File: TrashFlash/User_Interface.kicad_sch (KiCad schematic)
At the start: 15 parts, among them IC7 LP5024RSMR

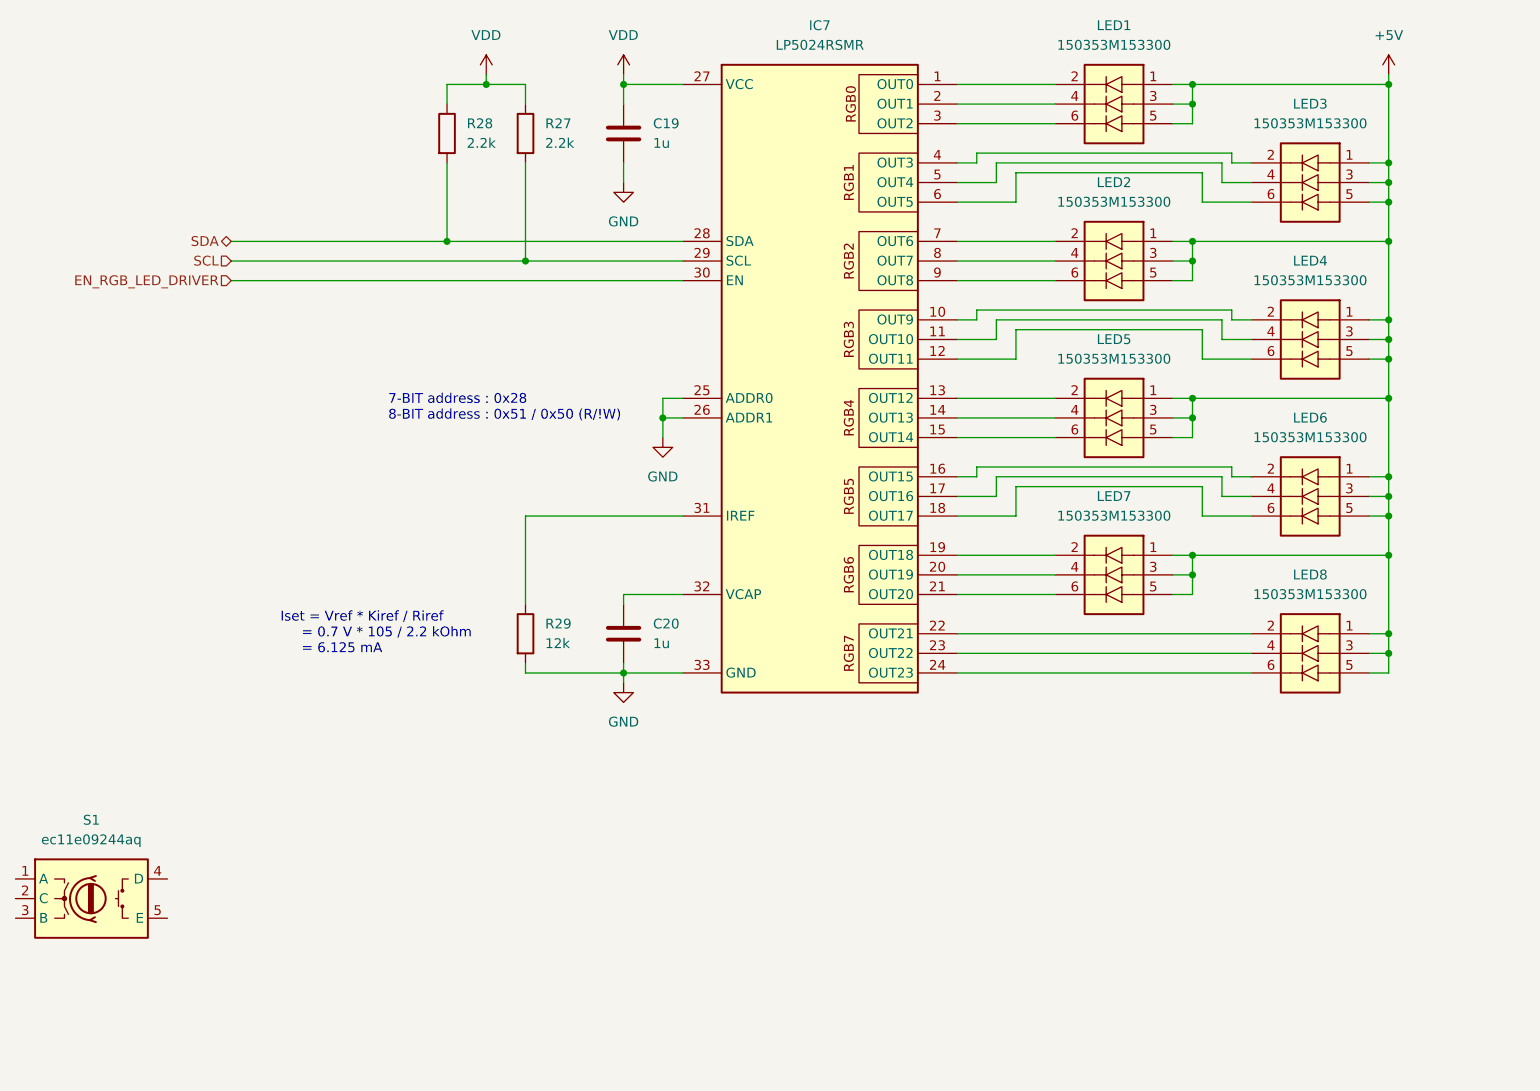
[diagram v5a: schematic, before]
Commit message: Added netlabels / cleaned up schematic
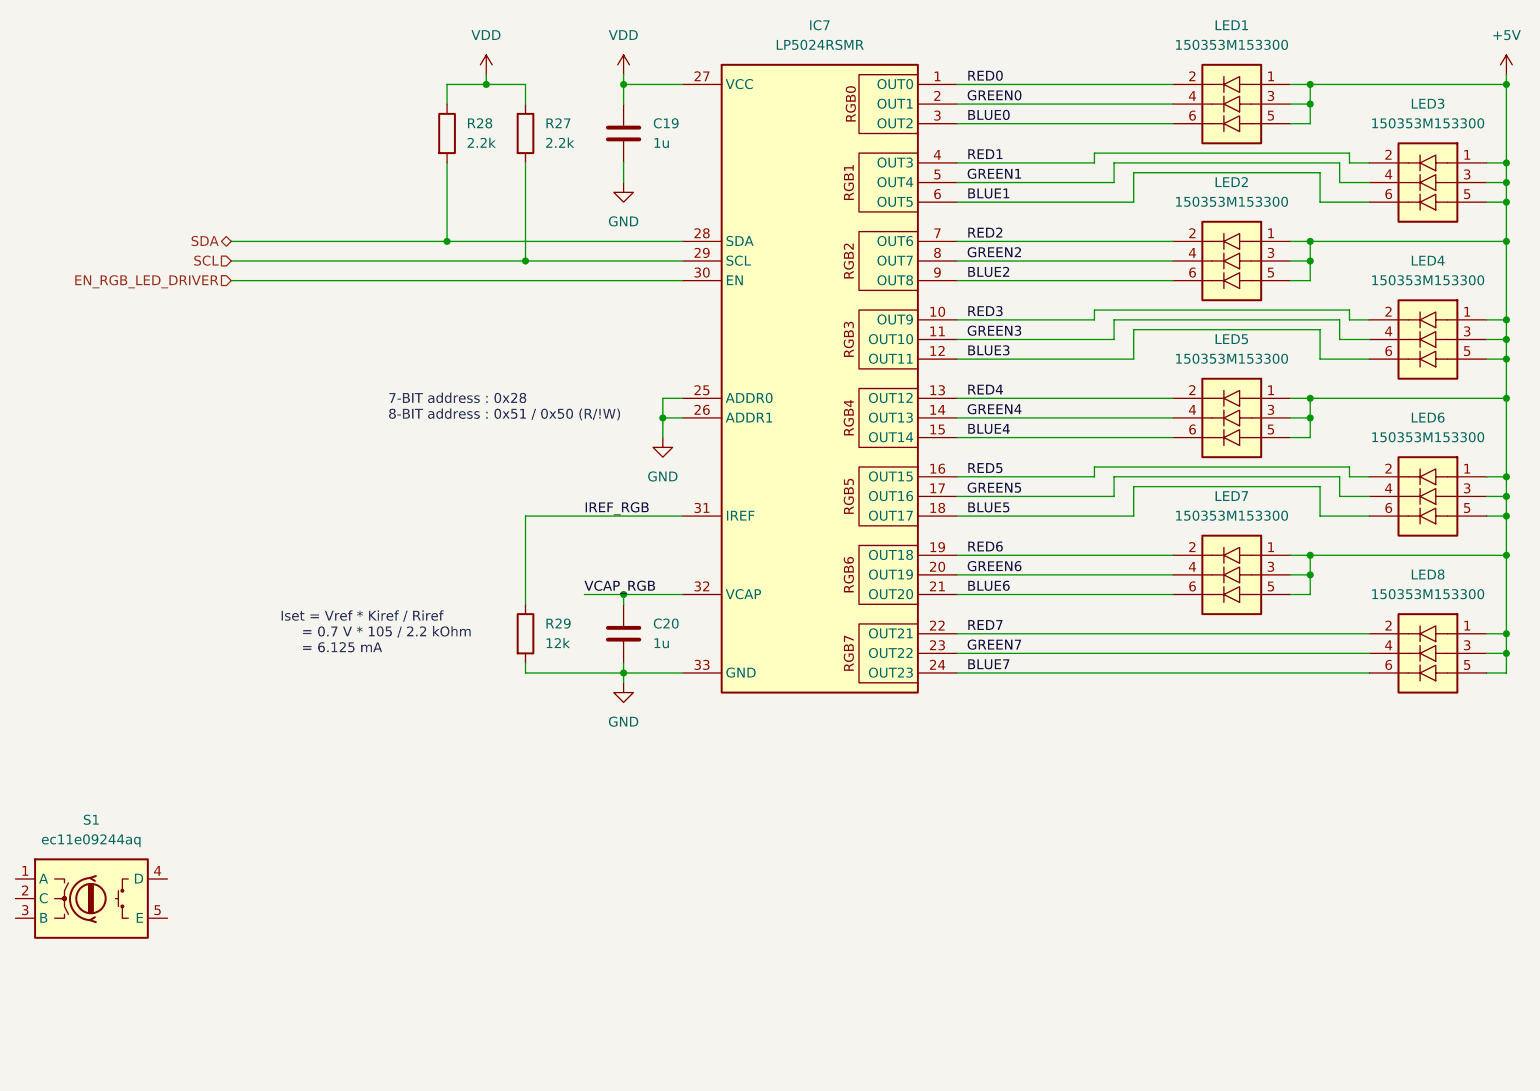
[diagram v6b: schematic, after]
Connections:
- net RED3: now reaches IC7.10 (OUT9), LED4.2 (K_RED)
- net GREEN3: now reaches IC7.11 (OUT10), LED4.4 (K_GREEN)
- net BLUE3: now reaches IC7.12 (OUT11), LED4.6 (K_BLUE)
- net RED2: now reaches IC7.7 (OUT6), LED2.2 (K_RED)
- net GREEN2: now reaches IC7.8 (OUT7), LED2.4 (K_GREEN)
- net BLUE2: now reaches IC7.9 (OUT8), LED2.6 (K_BLUE)
- net RED0: now reaches IC7.1 (OUT0), LED1.2 (K_RED)
- net RED4: now reaches IC7.13 (OUT12), LED5.2 (K_RED)
- net GREEN4: now reaches IC7.14 (OUT13), LED5.4 (K_GREEN)
- net BLUE4: now reaches IC7.15 (OUT14), LED5.6 (K_BLUE)
- net RED5: now reaches IC7.16 (OUT15), LED6.2 (K_RED)
- net GREEN5: now reaches IC7.17 (OUT16), LED6.4 (K_GREEN)
- net BLUE5: now reaches IC7.18 (OUT17), LED6.6 (K_BLUE)
- net RED6: now reaches IC7.19 (OUT18), LED7.2 (K_RED)
- net GREEN0: now reaches IC7.2 (OUT1), LED1.4 (K_GREEN)
- net GREEN6: now reaches IC7.20 (OUT19), LED7.4 (K_GREEN)
- net BLUE6: now reaches IC7.21 (OUT20), LED7.6 (K_BLUE)
- net RED7: now reaches IC7.22 (OUT21), LED8.2 (K_RED)
- net GREEN7: now reaches IC7.23 (OUT22), LED8.4 (K_GREEN)
- net BLUE7: now reaches IC7.24 (OUT23), LED8.6 (K_BLUE)
- net BLUE0: now reaches IC7.3 (OUT2), LED1.6 (K_BLUE)
- net IREF_RGB: now reaches IC7.31 (IREF), R29.1
- net VCAP_RGB: now reaches C20.1, IC7.32 (VCAP)
- net RED1: now reaches IC7.4 (OUT3), LED3.2 (K_RED)
- net GREEN1: now reaches IC7.5 (OUT4), LED3.4 (K_GREEN)
- net BLUE1: now reaches IC7.6 (OUT5), LED3.6 (K_BLUE)
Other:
- moved on the sheet: LED1, LED2, LED3, LED4, LED5, LED6, LED7, LED8

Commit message: Added 3D-models to footprints, PCB outline and component placement
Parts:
- IC7: footprint QFN40P400X400X100-33N-D -> TrashFlash:QFN40P400X400X100-33N-D
- LED1, LED2, LED3, LED4, LED5, LED6, LED7, LED8: footprint 150353M153300 -> TrashFlash:150353M153300
- S1: footprint ec11e09244aq -> TrashFlash:ec11e09244aq
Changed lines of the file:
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@@
 			)
 		)
-		(property "Footprint" "150353M153300"
+		(property "Footprint" "TrashFlash:150353M153300"
 			(at 217.17 166.04 0)
 			(effects
@@
 			)
 		)
-		(property "Footprint" "150353M153300"
+		(property "Footprint" "TrashFlash:150353M153300"
 			(at 191.77 155.88 0)
 			(effects
@@
 			)
 		)
-		(property "Footprint" "ec11e09244aq"
+		(property "Footprint" "TrashFlash:ec11e09244aq"
 			(at 48.26 143.51 0)
 			(effects
@@
 			)
 		)
-		(property "Footprint" "QFN40P400X400X100-33N-D"
+		(property "Footprint" "TrashFlash:QFN40P400X400X100-33N-D"
 			(at 138.43 127 0)
 			(effects
@@
 			)
 		)
-		(property "Footprint" "150353M153300"
+		(property "Footprint" "TrashFlash:150353M153300"
 			(at 217.17 186.36 0)
 			(effects
@@
 			)
 		)
-		(property "Footprint" "150353M153300"
+		(property "Footprint" "TrashFlash:150353M153300"
 			(at 191.77 176.2 0)
 			(effects
@@
 			)
 		)
-		(property "Footprint" "150353M153300"
+		(property "Footprint" "TrashFlash:150353M153300"
 			(at 217.17 145.72 0)
 			(effects
@@
 			)
 		)
-		(property "Footprint" "150353M153300"
+		(property "Footprint" "TrashFlash:150353M153300"
 			(at 217.17 206.68 0)
 			(effects
@@
 			)
 		)
-		(property "Footprint" "150353M153300"
+		(property "Footprint" "TrashFlash:150353M153300"
 			(at 191.77 135.56 0)
 			(effects
@@
 			)
 		)
-		(property "Footprint" "150353M153300"
+		(property "Footprint" "TrashFlash:150353M153300"
 			(at 191.77 196.52 0)
 			(effects

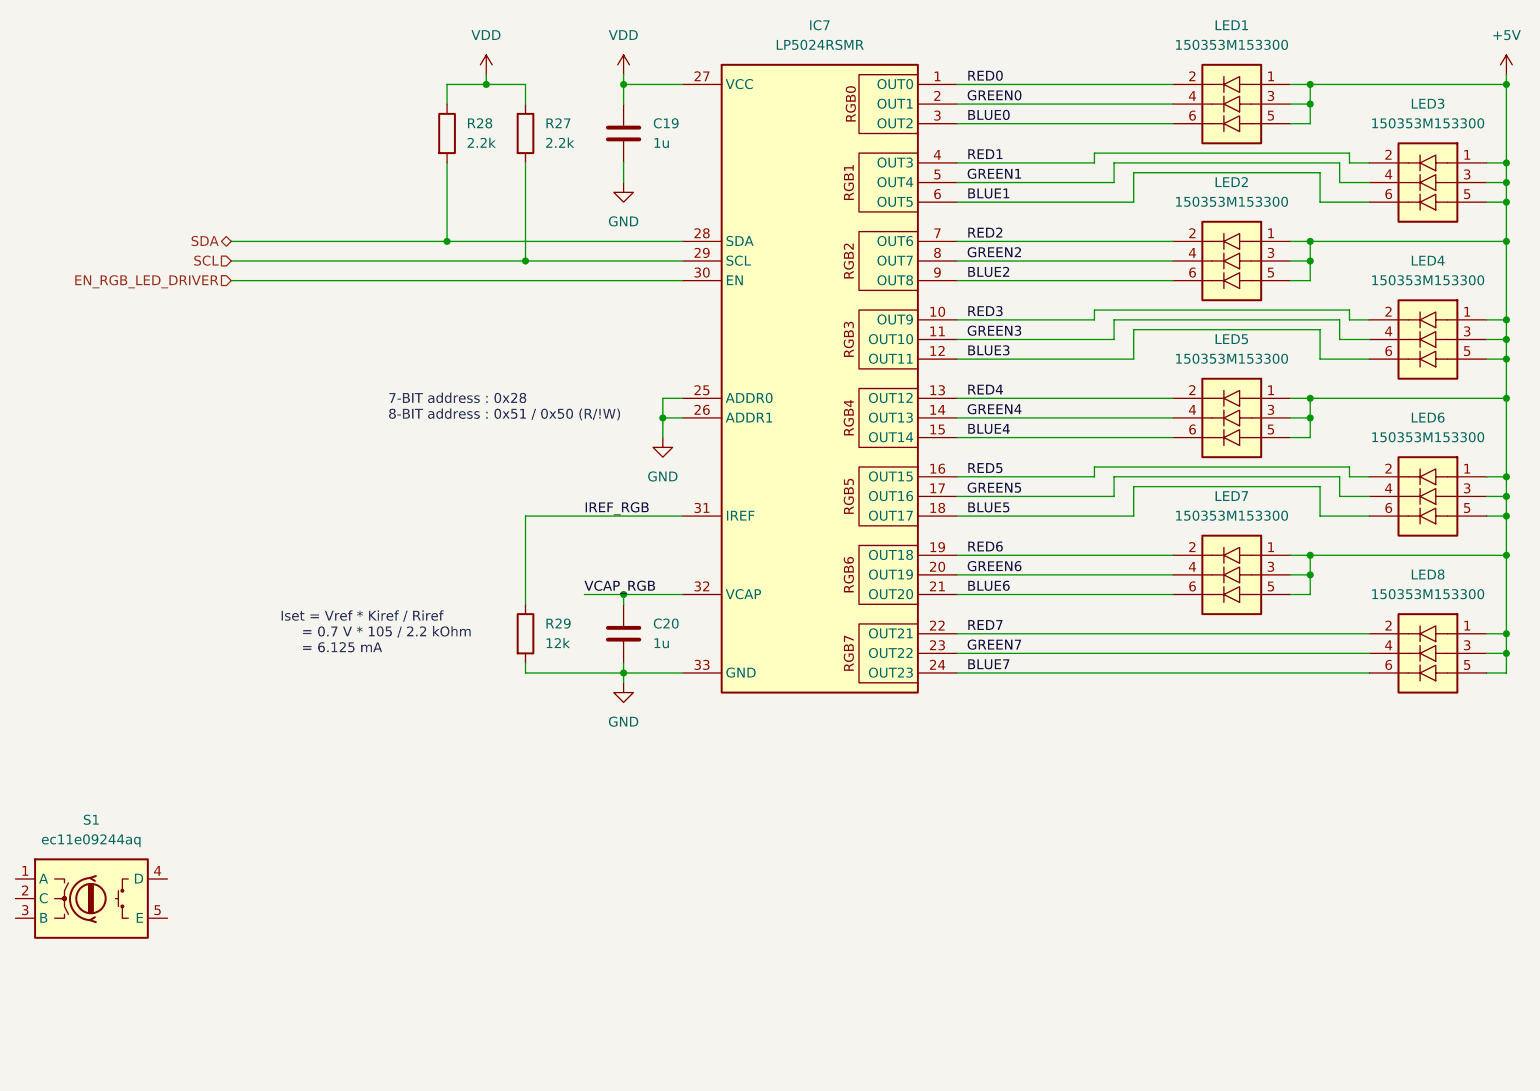
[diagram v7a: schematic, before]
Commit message: Added Wireless and inter PCB connector
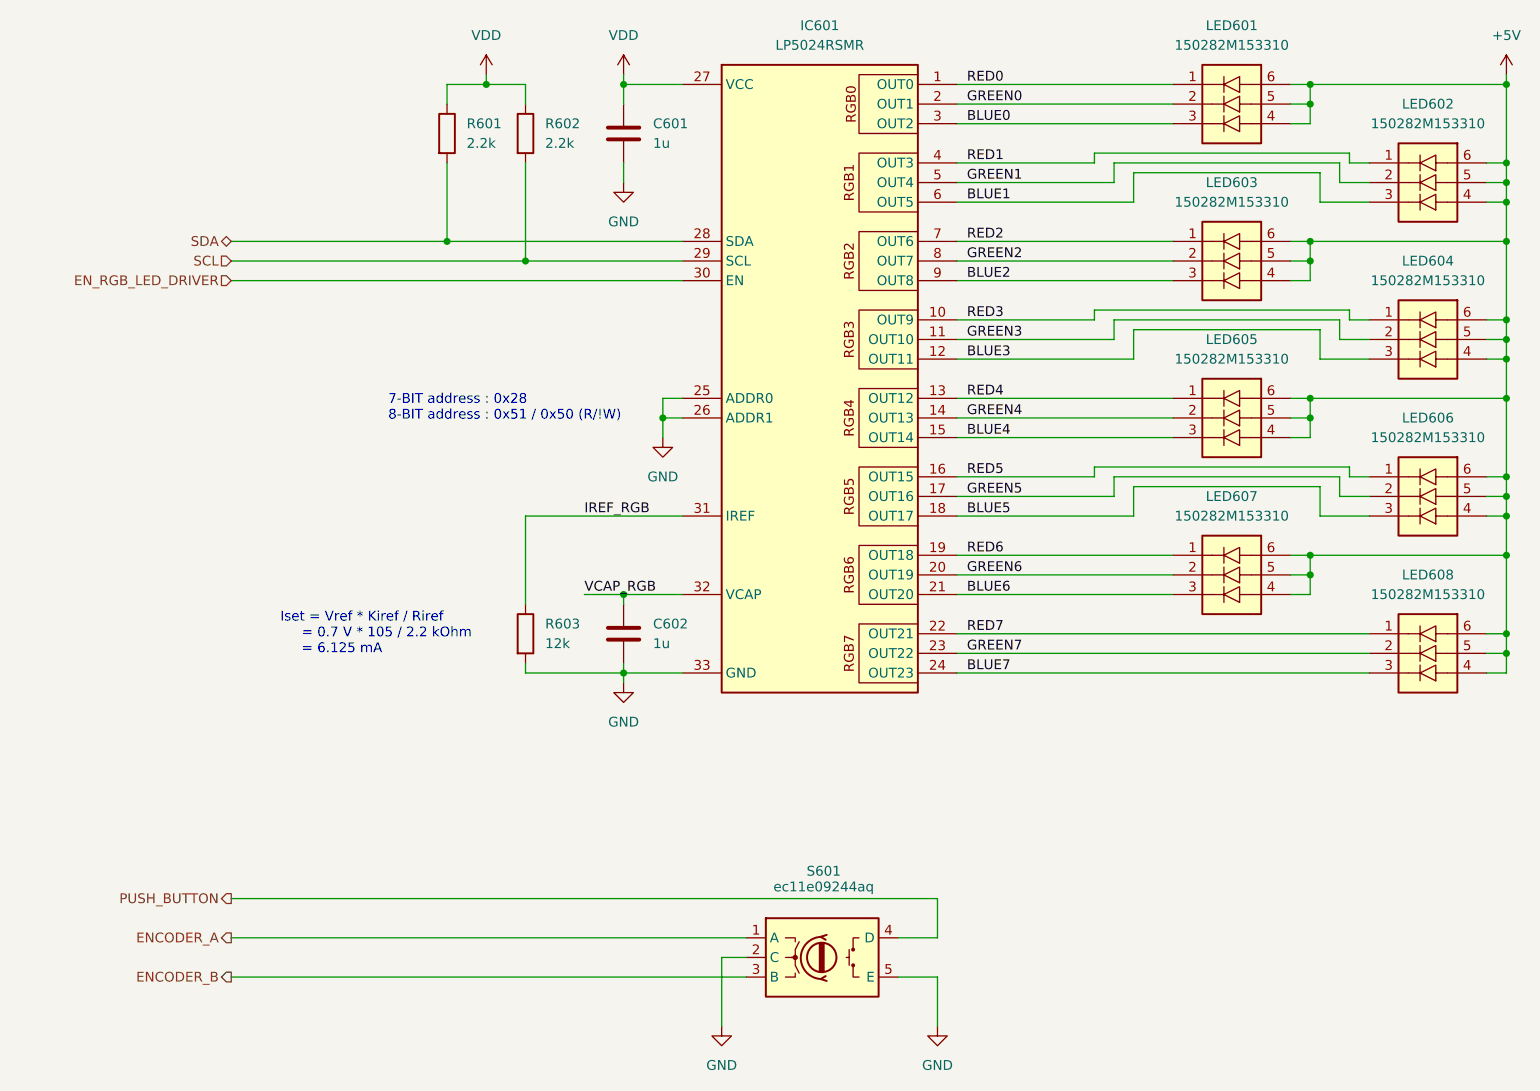
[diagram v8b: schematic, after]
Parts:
- removed LED1, LED2, LED3, LED4, LED5, LED6, LED7, LED8: 150353M153300, TrashFlash:150353M153300, symbol TrashFlash:150353M153300
- added LED601, LED602, LED603, LED604, LED605, LED606, LED607, LED608: 150282M153310, TrashFlash:150282M153310, symbol TrashFlash:150282M153310
- IC601: renamed from IC7; footprint TrashFlash:QFN40P400X400X100-33N-D -> QFN40P400X400X100-33N-D
- S601: renamed from S1; footprint TrashFlash:ec11e09244aq -> ec11e09244aq
- renumbered C19 to C601, C20 to C602, R28 to R601, R27 to R602, R29 to R603
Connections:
- net +5V: now also LED601.4 (A_BLUE), LED601.5 (A_GREEN), LED601.6 (A_RED), LED602.4 (A_BLUE), LED602.5 (A_GREEN), LED602.6 (A_RED), LED603.4 (A_BLUE), LED603.5 (A_GREEN), LED603.6 (A_RED), LED604.4 (A_BLUE), LED604.5 (A_GREEN), LED604.6 (A_RED), LED605.4 (A_BLUE), LED605.5 (A_GREEN), LED605.6 (A_RED), LED606.4 (A_BLUE), LED606.5 (A_GREEN), LED606.6 (A_RED), LED607.4 (A_BLUE), LED607.5 (A_GREEN), LED607.6 (A_RED), LED608.4 (A_BLUE), LED608.5 (A_GREEN), LED608.6 (A_RED)
- net BLUE0: now also LED601.3 (K_BLUE)
- net BLUE1: now also LED602.3 (K_BLUE)
- net BLUE2: now also LED603.3 (K_BLUE)
- net BLUE3: now also LED604.3 (K_BLUE)
- net BLUE4: now also LED605.3 (K_BLUE)
- net BLUE5: now also LED606.3 (K_BLUE)
- net BLUE6: now also LED607.3 (K_BLUE)
- net BLUE7: now also LED608.3 (K_BLUE)
- net GND: now also S601.2 (C), S601.5 (E)
- net GREEN0: now also LED601.2 (K_GREEN)
- net GREEN1: now also LED602.2 (K_GREEN)
- net GREEN2: now also LED603.2 (K_GREEN)
- net GREEN3: now also LED604.2 (K_GREEN)
- net GREEN4: now also LED605.2 (K_GREEN)
- net GREEN5: now also LED606.2 (K_GREEN)
- net GREEN6: now also LED607.2 (K_GREEN)
- net GREEN7: now also LED608.2 (K_GREEN)
- net RED0: now also LED601.1 (K_RED)
- net RED1: now also LED602.1 (K_RED)
- net RED2: now also LED603.1 (K_RED)
- net RED3: now also LED604.1 (K_RED)
- net RED4: now also LED605.1 (K_RED)
- net RED5: now also LED606.1 (K_RED)
- net RED6: now also LED607.1 (K_RED)
- net RED7: now also LED608.1 (K_RED)
- net ENCODER_A: now reaches S601.1 (A)
- net ENCODER_B: now reaches S601.3 (B)
- net PUSH_BUTTON: now reaches S601.4 (D)
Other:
- moved on the sheet: S601
